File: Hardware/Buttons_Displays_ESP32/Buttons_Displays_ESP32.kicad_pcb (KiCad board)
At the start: 2 copper layers, 70.5 x 61.8 mm, 28 parts, among them J1 Conn_01x09, J2 Conn_01x09, J3 Conn_01x09, J4 Conn_01x09, J5 i2c, J6 USB_C_Receptacle_USB2.0_16P, SW1 SW_Push, SW2 SW_Push, U1 ESP32-S3-WROOM-1, U2 USBLC6-2P6

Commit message: Update Buttons_Displays_ESP32.kicad_pcb
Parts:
- moved REF** 5.90 mm to (163.8, 53.2)
- moved REF** 5.90 mm to (100.8, 53.2)
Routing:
- net GND: vias 108 -> 107
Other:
- board size 70.5 x 61.8 mm -> 70.5 x 55.4 mm
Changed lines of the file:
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@@
 		(tags "Connector")
 		(property "Reference" "J5"
-			(at -11.05 6.925 360)
+			(at -11.05 6.925 0)
 			(layer "F.SilkS")
 			(effects
@@
 	(footprint "MountingHole:MountingHole_3.2mm_M3_DIN965_Pad"
 		(layer "F.Cu")
-		(at 163.7 47.3)
+		(at 163.8 53.2)
 		(descr "Mounting Hole 3.2mm, M3, DIN965")
 		(tags "mounting hole 3.2mm m3 din965")
@@
 	(footprint "MountingHole:MountingHole_3.2mm_M3_DIN965_Pad"
 		(layer "F.Cu")
-		(at 100.7 47.3)
+		(at 100.8 53.2)
 		(descr "Mounting Hole 3.2mm, M3, DIN965")
 		(tags "mounting hole 3.2mm m3 din965")
@@
 	)
 	(gr_rect
-		(start 97.25 43.25)
+		(start 97.25 49.65)
 		(end 167.75 105)
 		(stroke
@@
 		(size 0.6)
 		(drill 0.3)
-		(layers "F.Cu" "B.Cu")
-		(free yes)
-		(net 2)
-	)
-	(via
-		(at 161.1 96.78)
-		(size 0.6)
-		(drill 0.3)

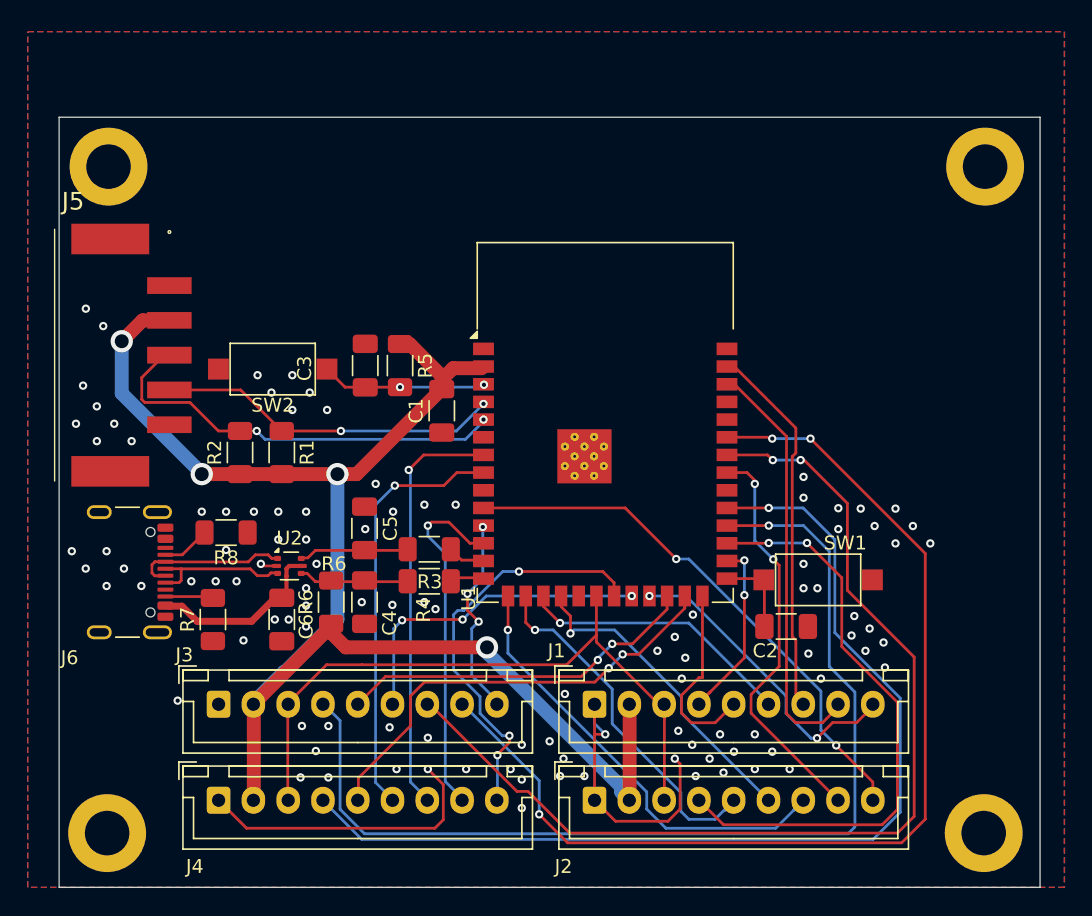
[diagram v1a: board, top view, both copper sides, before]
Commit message: hoogte aangepast
hoogte pcb is nu 55mm
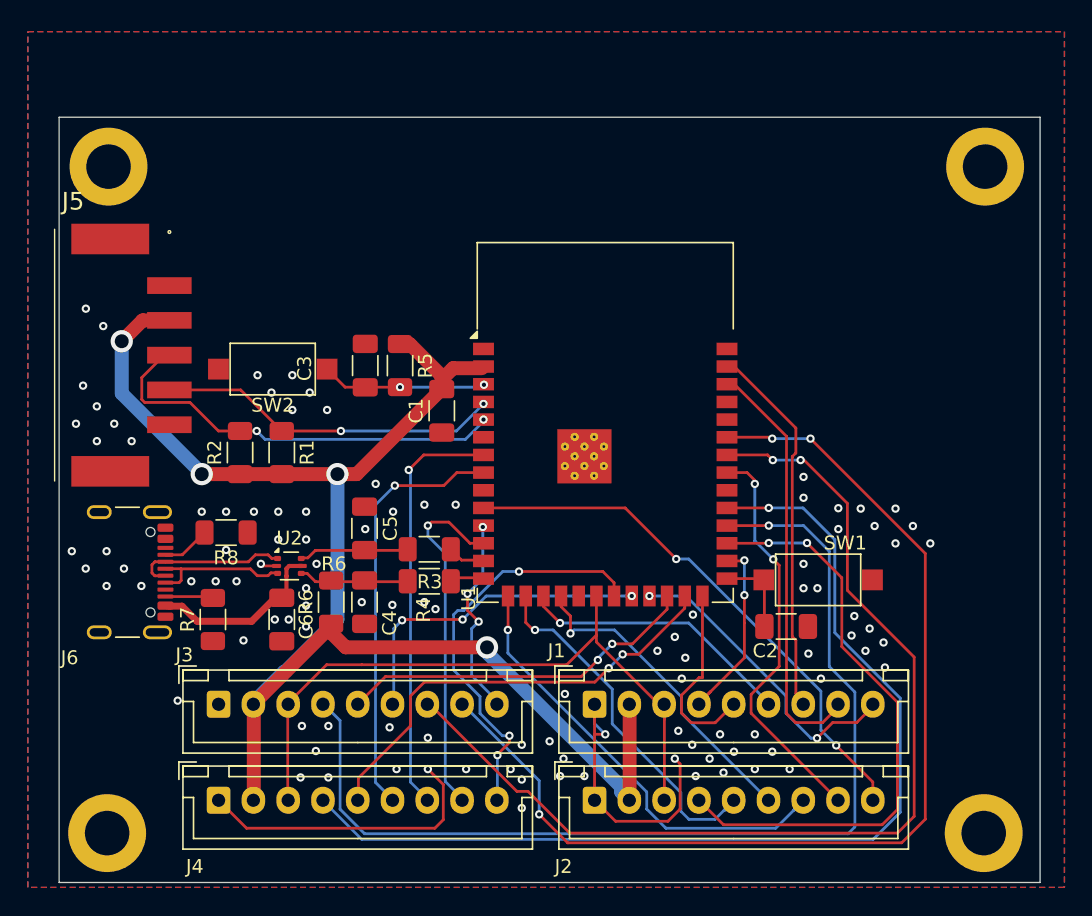
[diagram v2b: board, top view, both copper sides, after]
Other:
- board size 70.5 x 55.4 mm -> 70.5 x 55 mm
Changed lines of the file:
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@@
 	(gr_rect
 		(start 97.25 49.65)
-		(end 167.75 105)
+		(end 167.75 104.65)
 		(stroke
 			(width 0.05)

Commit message: Silkscreen aangepast
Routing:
- net +5Vout: track 12.2 -> 18.9 mm
- net GND: track 43.6 -> 46.3 mm, vias 107 -> 106
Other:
- board size 70.5 x 55 mm -> 70 x 55 mm
- board text added: "Display & Buttons ESP32 Module V1.0"
- board text added: "Made by ESE For project APPS"
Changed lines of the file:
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@@
 		(tags "Connector")
 		(property "Reference" "J5"
-			(at -11.05 6.925 0)
+			(at -11 -1.375 0)
 			(layer "F.SilkS")
 			(effects
@@
 		(tags "resistor handsolder")
 		(property "Reference" "R4"
-			(at 0.41 -2.06 90)
+			(at -0.05 -1.8 180)
 			(layer "F.SilkS")
 			(effects
@@
 		(tags "capacitor handsolder")
 		(property "Reference" "C5"
-			(at 0 -1.85 90)
+			(at 0.1 1.8 90)
 			(layer "F.SilkS")
 			(effects
@@
 		(tags "resistor handsolder")
 		(property "Reference" "R8"
-			(at 0 -1.82 0)
+			(at 0.05 1.75 0)
 			(layer "F.SilkS")
 			(effects
@@
 		(tags "capacitor handsolder")
 		(property "Reference" "C1"
-			(at 0 -1.85 90)
+			(at -0.15 -1.95 -90)
 			(layer "F.SilkS")
 			(effects
@@
 		(tags "resistor handsolder")
 		(property "Reference" "R3"
-			(at -0.03 -2.34 0)
+			(at 0.05 1.7 0)
 			(layer "F.SilkS")
 			(effects
@@
 		(tags "capacitor handsolder")
 		(property "Reference" "C6"
-			(at 0.51 -1.75 90)
+			(at -0.05 1.85 -90)
 			(layer "F.SilkS")
 			(effects
@@
 		(tags "resistor handsolder")
 		(property "Reference" "R5"
-			(at 0 -1.82 90)
+			(at -1.65 -2.1 180)
 			(layer "F.SilkS")
 			(effects
@@
 		(tags "capacitor handsolder")
 		(property "Reference" "C3"
-			(at -0.2 -4.36 90)
+			(at -3.25 0.05 180)
 			(layer "F.SilkS")
 			(effects
@@
 		(tags "2.4 GHz Wi-Fi and Bluetooth module")
 		(property "Reference" "U1"
-			(at -9.82 12.63 90)
+			(at -9.2 14.19 0)
 			(unlocked yes)
 			(layer "F.SilkS")
@@
 		(tags "connector JST XH vertical")
 		(property "Reference" "J1"
-			(at -2.73 -3.84 0)
+			(at -2.73 -3.64 0)
 			(layer "F.SilkS")
 			(effects
@@
 		(tags "USB C Type-C Receptacle SMD USB 2.0 16P 16C USB4105-15-A USB4105-15-A-060 USB4105-15-A-120 USB4105-GF-A USB4105-GF-A-060 USB4105-GF-A-120")
 		(property "Reference" "J6"
-			(at 6.15 3.21 0)
+			(at 6.15 2.31 0)
 			(unlocked yes)
 			(layer "F.SilkS")
@@
 	(gr_rect
 		(start 97.25 49.65)
-		(end 167.75 104.65)
+		(end 167.25 104.65)
 		(stroke
 			(width 0.05)
@@
 		(layer "Edge.Cuts")
 	)
+	(gr_text "Made by ESE\nFor project APPS"
+		(at 166 57 90)
+		(layer "B.SilkS")
+		(effects
+			(font
+				(size 1.5 1.5)
+				(thickness 0.3)
+				(bold yes)
+			)
+			(justify left bottom mirror)
+		)
+	)
+	(gr_text "Display & Buttons ESP32 Module V1.0\n"
+		(at 114 53.5 0)
+		(layer "F.SilkS")
+		(effects
+			(font
+				(size 1.5 1.5)
+				(thickness 0.3)
+				(bold yes)
+			)
+			(justify left bottom)
+		)
+	)
 	(gr_text "C4\n"
-		(at 121 86 90)
+		(at 121 84.85 90)
 		(layer "F.SilkS")
 		(effects
@@
 	)
 	(segment
+		(start 104.89 85.55)
+		(end 104.89 86.095)
+		(width 0.2)
+		(layer "F.Cu")
+		(net 2)
+	)
+	(segment
 		(start 124.86 100.14)
 		(end 124.86 97.61)
@@
 	)
 	(segment
+		(start 104.89 86.095)
+		(end 104.315 86.67)
+		(width 0.2)
+		(layer "F.Cu")
+		(net 2)
+	)
+	(segment
 		(start 111.9 81.9)
 		(end 112.875 81.9)
@@
 	)
 	(segment
+		(start 104.89 78.605)
+		(end 104.315 78.03)
+		(width 0.2)
+		(layer "F.Cu")
+		(net 2)
+	)
+	(segment
 		(start 124.25 100.75)
 		(end 124.86 100.14)
@@
 	)
 	(segment
+		(start 104.89 79.15)
+		(end 104.89 78.605)
+		(width 0.2)
+		(layer "F.Cu")
+		(net 2)
+	)
+	(segment
 		(start 135.73 94)
 		(end 135.73 98.74)
@@
 	)
 	(via
+		(at 154.25 89.25)
+		(size 0.6)
+		(drill 0.3)
+		(layers "F.Cu" "B.Cu")
+		(free yes)
+		(net 2)
+	)
+	(via
 		(at 123.5 84.5)
 		(size 0.6)
@@
 	)
 	(via
-		(at 156.5 87.4)
-		(size 0.6)
-		(drill 0.3)
-		(layers "F.Cu" "B.Cu")
-		(free yes)
-		(net 2)
-	)
-	(via
 		(at 102.46 72.93)
 		(size 0.6)
@@
 	)
 	(via
-		(at 154.4 85.5)
+		(at 106.2 53.95)
 		(size 0.6)
 		(drill 0.3)
@@
 	)
 	(via
+		(at 153.25 88.15)
+		(size 0.6)
+		(drill 0.3)
+		(layers "F.Cu" "B.Cu")
+		(free yes)
+		(net 2)
+	)
+	(via
 		(at 111.25 78)
 		(size 0.6)
@@
 	)
 	(via
-		(at 155.5 86.4)
-		(size 0.6)
-		(drill 0.3)
-		(layers "F.Cu" "B.Cu")
-		(free yes)
-		(net 2)
-	)
-	(via
 		(at 125.75 77.5)
 		(size 0.6)
@@
 	)
 	(via
-		(at 103.16 83.34)
-		(size 0.6)
-		(drill 0.3)
-		(layers "F.Cu" "B.Cu")
-		(free yes)
-		(net 2)
-	)
-	(via
 		(at 150.75 75.5)
 		(size 0.6)
@@
 	)
 	(segment
+		(start 104.279594 79.95)
+		(end 104.89 79.95)
+		(width 0.2)
+		(layer "F.Cu")
+		(net 12)
+	)
+	(segment
+		(start 103.52 80.709594)
+		(end 104.279594 79.95)
+		(width 0.2)
+		(layer "F.Cu")
+		(net 12)
+	)
+	(segment
 		(start 105.0625 84.79)
 		(end 106.0825 84.79)
@@
 	)
 	(segment
+		(start 103.52 83.97)
+		(end 103.52 80.709594)
+		(width 0.2)
+		(layer "F.Cu")
+		(net 12)
+	)
+	(segment
+		(start 104.3 84.75)
+		(end 103.52 83.97)
+		(width 0.2)
+		(layer "F.Cu")
+		(net 12)
+	)
+	(segment
 		(start 111.0875 85.88)
 		(end 112.9 84.0675)
@@
 	)
 	(segment
+		(start 104.89 84.75)
+		(end 104.3 84.75)
+		(width 0.2)
+		(layer "F.Cu")
+		(net 12)
+	)
+	(segment
 		(start 133.25 86)
 		(end 132.055 84.805)
@@
 	)
 	(segment
-		(start 153.5 87.7)
-		(end 153.5 82.75)
+		(start 157.5 99.4)
+		(end 157.5 88.05)
 		(width 0.2)
 		(layer "F.Cu")
@@
 	)
 	(segment
-		(start 156.4 100.5)
-		(end 157.5 99.4)
+		(start 145 100.5)
+		(end 156.4 100.5)
 		(width 0.2)
 		(layer "F.Cu")
@@
 	)
 	(segment
-		(start 148.23 80.27)
-		(end 145.25 80.27)
+		(start 153.5 84.05)
+		(end 153.5 82.75)
 		(width 0.2)
 		(layer "F.Cu")
@@
 	)
 	(segment
-		(start 148.25 80.25)
-		(end 148.23 80.27)
+		(start 148.23 80.27)
+		(end 145.25 80.27)
 		(width 0.2)
 		(layer "F.Cu")
@@
 	)
 	(segment
-		(start 143.25 98.75)
-		(end 145 100.5)
+		(start 148.25 80.25)
+		(end 148.23 80.27)
 		(width 0.2)
 		(layer "F.Cu")
@@
 	)
 	(segment
-		(start 145 100.5)
-		(end 156.4 100.5)
+		(start 157.5 88.05)
+		(end 153.5 84.05)
 		(width 0.2)
 		(layer "F.Cu")
@@
 	)
 	(segment
-		(start 157.5 99.4)
-		(end 157.5 91.7)
+		(start 156.4 100.5)
+		(end 157.5 99.4)
 		(width 0.2)
 		(layer "F.Cu")
@@
 	)
 	(segment
-		(start 157.5 91.7)
-		(end 153.5 87.7)
+		(start 143.25 98.75)
+		(end 145 100.5)
 		(width 0.2)
 		(layer "F.Cu")

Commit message: geber files
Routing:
- net GND: vias 106 -> 105
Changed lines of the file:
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@@
 			(outputformat 1)
 			(mirror no)
-			(drillshape 1)
+			(drillshape 0)
 			(scaleselection 1)
-			(outputdirectory "")
+			(outputdirectory "Gerber/")
 		)
 	)
@@
 		(size 0.6)
 		(drill 0.3)
-		(layers "F.Cu" "B.Cu")
-		(free yes)
-		(net 2)
-	)
-	(via
-		(at 105.77 91.58)
-		(size 0.6)
-		(drill 0.3)
